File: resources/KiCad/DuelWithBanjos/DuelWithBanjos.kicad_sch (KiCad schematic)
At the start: 4 parts, among them U1 ESP32-WROOM-32

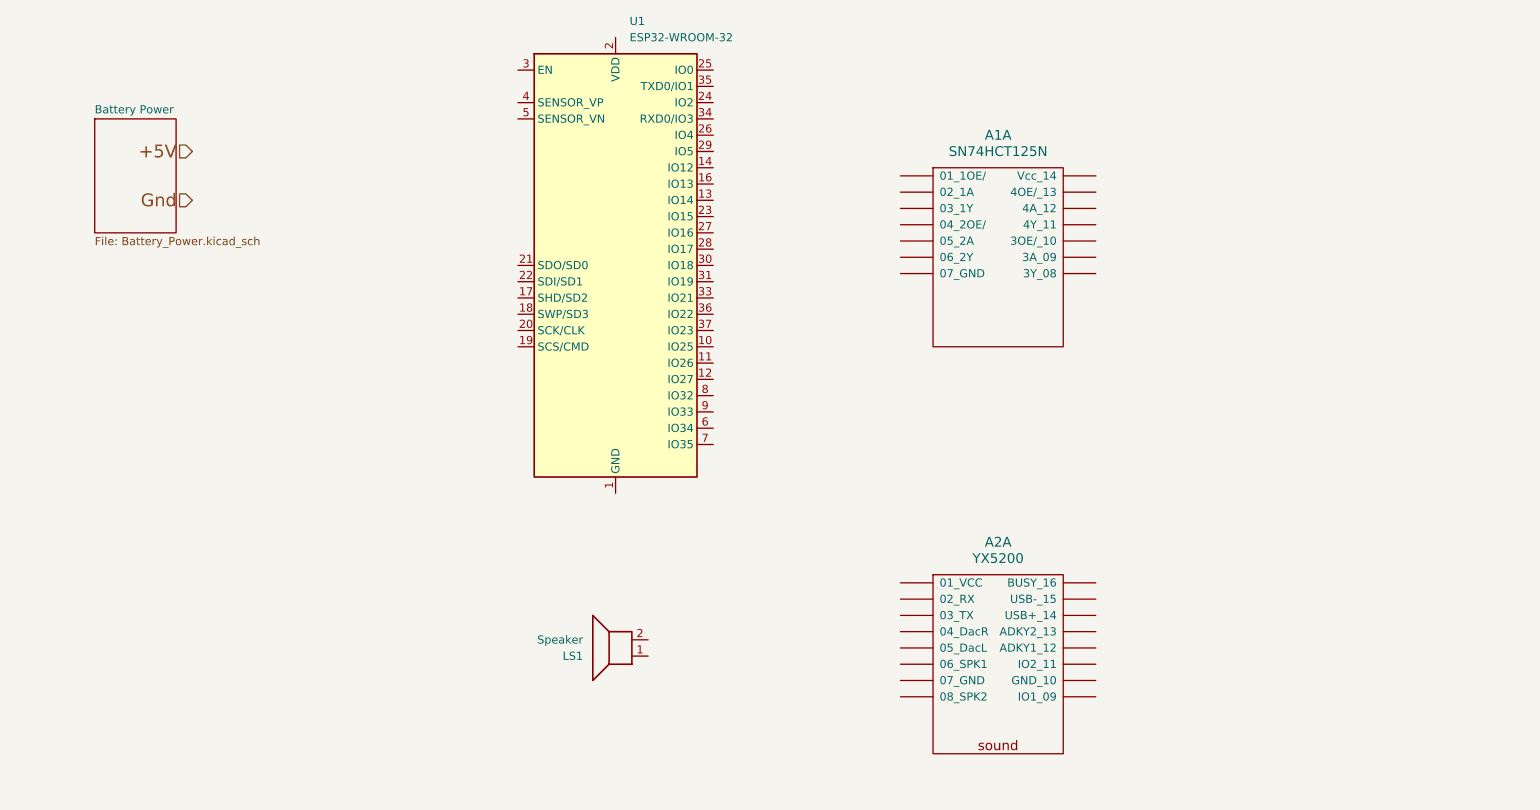
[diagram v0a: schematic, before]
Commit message: pin assignments and schematic first cut
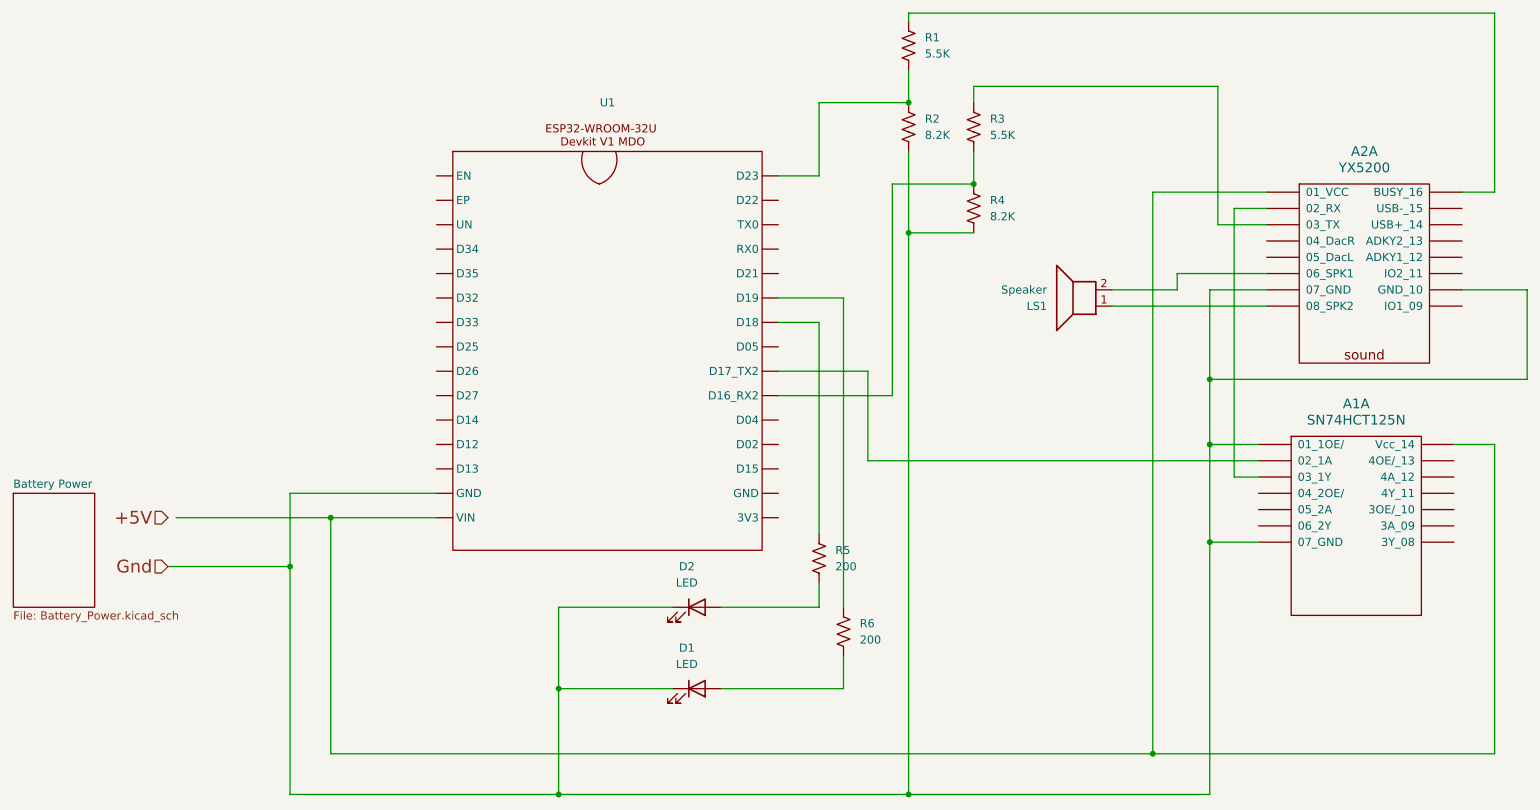
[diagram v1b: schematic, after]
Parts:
- removed U1: ESP32-WROOM-32, RF_Module:ESP32-WROOM-32, symbol RF_Module:ESP32-WROOM-32
- added D1, D2: LED, symbol Device:LED
- added R1, R3: 5.5K, symbol Device:R_US
- added R2, R4: 8.2K, symbol Device:R_US
- added R5, R6: 200, symbol Device:R_US
- added U1: ~, symbol mdoLibrary:mdo_esp32_wroom
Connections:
- net Gnd : now also A1.~ (Vcc_14), A2.~ (USB-_15), D1.1 (K), D2.1 (K), R2.2, R4.2, U1. (VIN)
- net at LS1.1: now also A2.~ (USB-_15)
- net at LS1.2: now also A2.~ (USB-_15)
- new net: R1.2, R2.1, U1. (VIN)
- new net: A2.~ (USB-_15), R3.1
- new net: R3.2, R4.1, U1. (VIN)
- new net: R5.1, U1. (VIN)
- new net: A1.~ (Vcc_14), U1. (VIN)
- new net: A1.~ (Vcc_14), A2.~ (USB-_15), U1. (VIN)
- new net: R6.1, U1. (VIN)
- new net: D2.2 (A), R5.2
- new net: A1.~ (Vcc_14), A2.~ (USB-_15)
- new net: A2.~ (USB-_15), R1.1
- new net: D1.2 (A), R6.2
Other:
- moved on the sheet: A1A, A2A, LS1

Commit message: update schematic
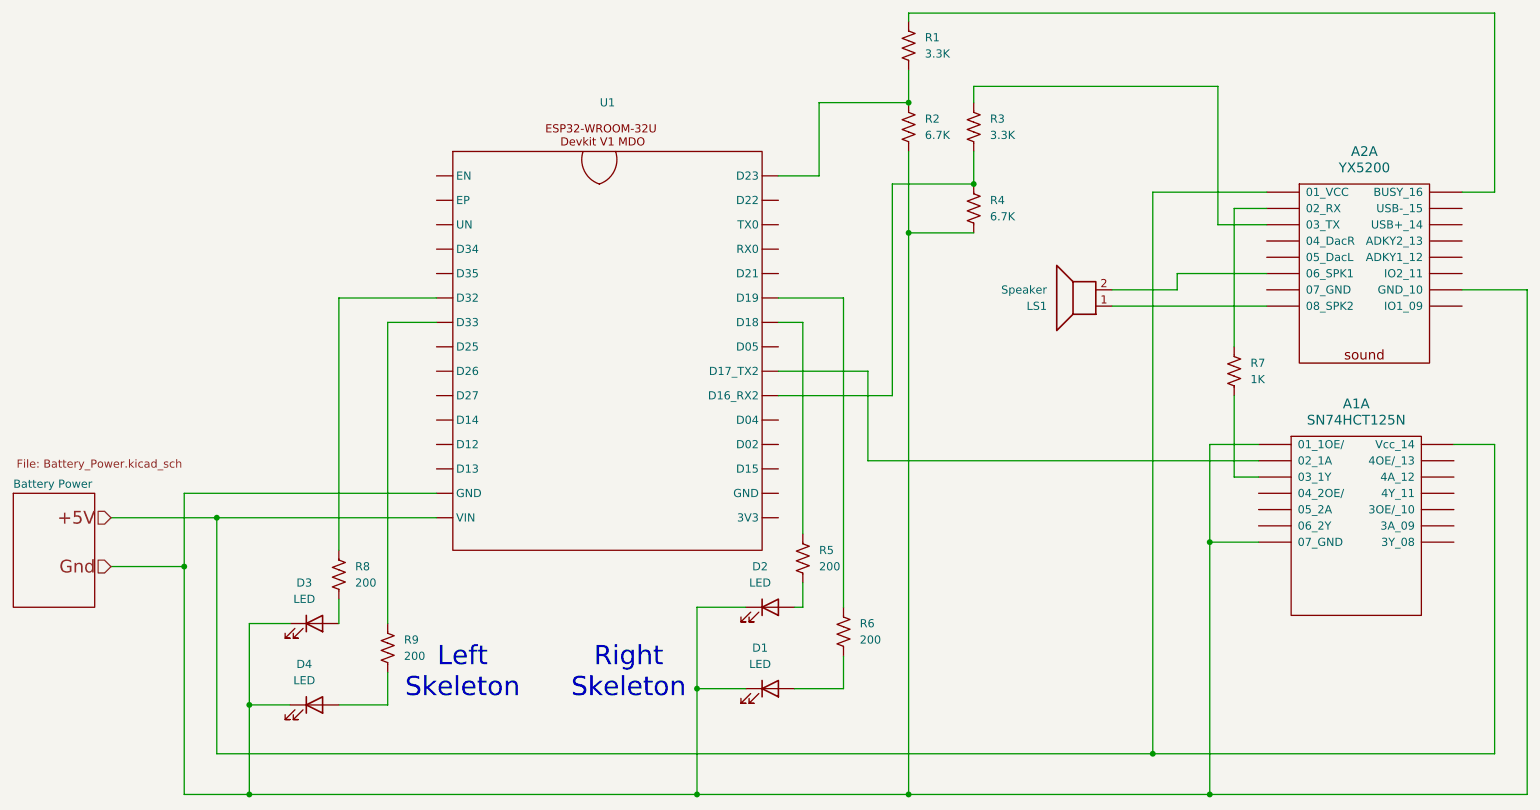
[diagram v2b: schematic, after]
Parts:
- added D3, D4: LED, symbol Device:LED
- added R7: 1K, symbol Device:R_US
- added R8, R9: 200, symbol Device:R_US
- R1, R3: value 5.5K -> 3.3K
- R2, R4: value 8.2K -> 6.7K
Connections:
- net +5V : now also A1.~ (Vcc_14), A2.~ (USB-_15), U1. (VIN)
- net Gnd : now also D3.1 (K), D4.1 (K)
- new net: R9.1, U1. (VIN)
- new net: D4.2 (A), R9.2
- new net: R8.1, U1. (VIN)
- new net: D3.2 (A), R8.2
- new net: A2.~ (USB-_15), R7.1
- new net: A1.~ (Vcc_14), R7.2
- new net: A1.~ (Vcc_14), U1. (VIN)
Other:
- note added: "Left Skeleton"
- note added: "Right Skeleton"
- moved on the sheet: D1, D2, R5

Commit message: add connectors for skeletons, move deck chairs around
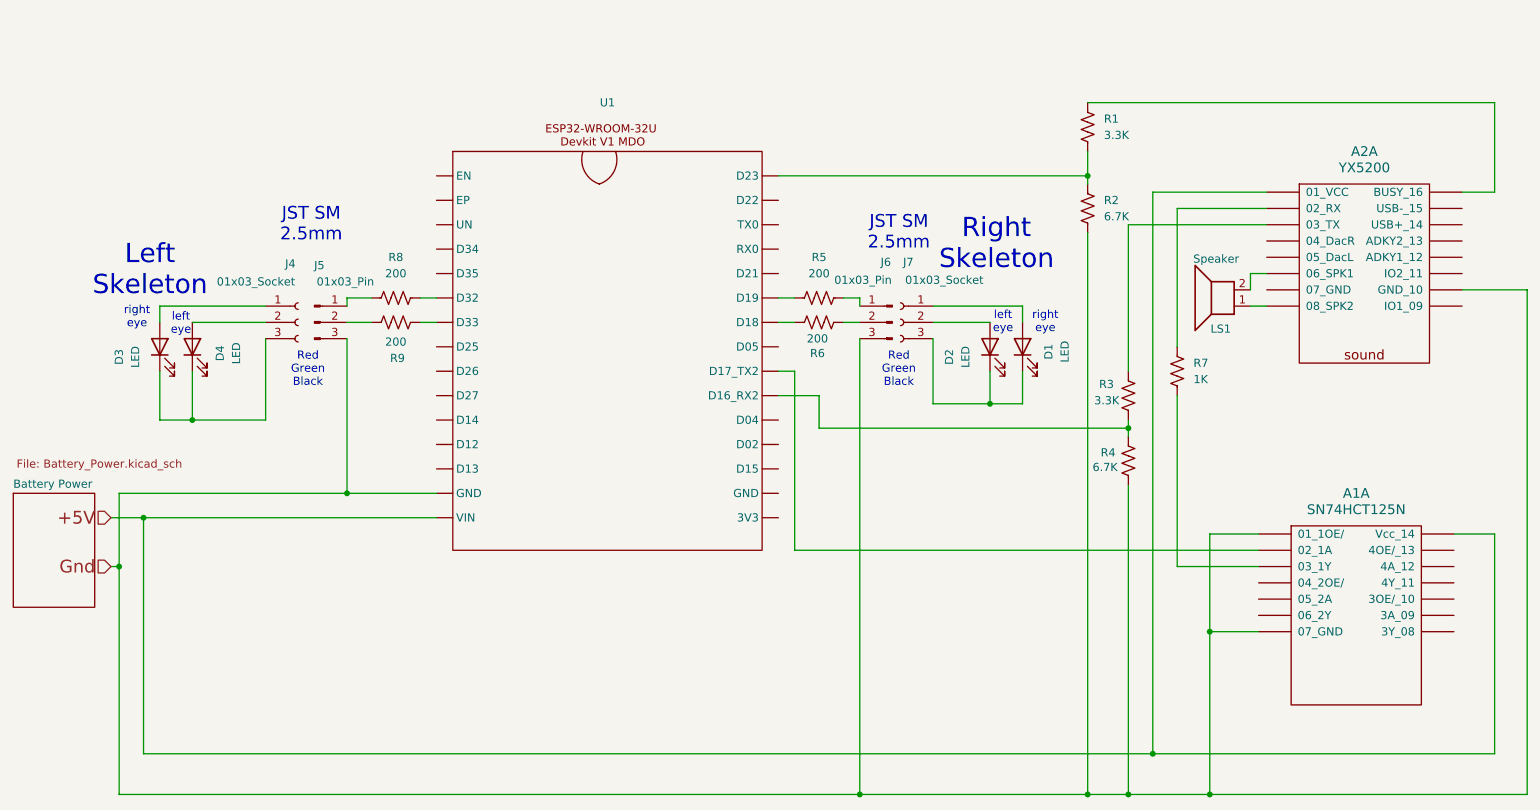
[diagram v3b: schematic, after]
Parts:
- added J4, J7: 01x03_Socket, symbol Connector:Conn_01x03_Socket
- added J5, J6: 01x03_Pin, symbol Connector:Conn_01x03_Pin
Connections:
- net Gnd : now also J5.3 (Pin_3), J6.3 (Pin_3); no longer D1.1 (K), D2.1 (K), D3.1 (K), D4.1 (K)
- net at R9.2: now also J5.2 (Pin_2); no longer D4.2 (A)
- net at R8.2: now also J5.1 (Pin_1); no longer D3.2 (A)
- net at R5.1: now also J6.1 (Pin_1); no longer U1. (VIN)
- net at R6.1: now also J6.2 (Pin_2); no longer U1. (VIN)
- net at R5.2: now also U1. (VIN); no longer D2.2 (A)
- net at R6.2: now also U1. (VIN); no longer D1.2 (A)
- new net: D3.1 (K), D4.1 (K), J4.3 (Pin_3)
- new net: D4.2 (A), J4.2 (Pin_2)
- new net: A1.~ (Vcc_14), U1. (VIN)
- new net: D3.2 (A), J4.1 (Pin_1)
- new net: D1.1 (K), D2.1 (K), J7.3 (Pin_3)
- new net: D2.2 (A), J7.2 (Pin_2)
- new net: D1.2 (A), J7.1 (Pin_1)
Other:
- note added: "JST SM 2.5mm"
- note added: "Red Green Black"
- note added: "left eye"
- note added: "right eye"
- moved on the sheet: A1A, D1, D2, D3, D4, LS1, R1, R2, R3, R4, R5, R6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

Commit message: move pins farther apart
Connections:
- new net: A1.~ (Vcc_14), U1. (VIN)
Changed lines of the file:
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@@
 	(title_block
 		(title "DuelWithBanjos")
-		(date "2025-04-10")
+		(date "2025-04-13")
 		(rev "Rev 0.9")
 		(company "https://github.com/Mark-MDO47")
@@
 	(wire
 		(pts
+			(xy 83.82 80.01) (xy 83.82 87.63)
+		)
+		(stroke
+			(width 0)
+			(type default)
+		)
+	)
+	(wire
+		(pts
 			(xy 187.96 53.34) (xy 187.96 57.15)
 		)
@@
 	(wire
 		(pts
+			(xy 86.36 87.63) (xy 83.82 87.63)
+		)
+		(stroke
+			(width 0)
+			(type default)
+		)
+	)
+	(wire
+		(pts
 			(xy 36.83 118.11) (xy 36.83 153.67)
 		)
 		(stroke
-			(width 0)
-			(type default)
-		)
-	)
-	(wire
-		(pts
-			(xy 83.82 80.01) (xy 86.36 80.01)
-		)
-		(stroke

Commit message: KiCad V9.0.1
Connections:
- new net: A1.~ (3Y_08), U1. (3V3)
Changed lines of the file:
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@@
 (kicad_sch
-	(version 20231120)
+	(version 20250114)
 	(generator "eeschema")
-	(generator_version "8.0")
+	(generator_version "9.0")
 	(paper "USLetter")
 	(title_block
 		(title "DuelWithBanjos")
-		(date "2025-04-13")
+		(date "2025-05-08")
 		(rev "Rev 0.9")
 		(company "https://github.com/Mark-MDO47")
 	)
+	(text "Red\nGreen\nBlack"
+		(exclude_from_sim no)
+		(at 66.294 87.376 0)
+		(effects
+			(font
+				(size 1.27 1.27)
+			)
+		)
+	)
+	(text "Right\nSkeleton"
+		(exclude_from_sim no)
+		(at 173.736 67.818 0)
+		(effects
+			(font
+				(size 3 3)
+			)
+		)
+	)
+	(text "right\neye"
+		(exclude_from_sim no)
+		(at 39.624 79.248 0)
+		(effects
+			(font
+				(size 1.27 1.27)
+			)
+		)
+	)
+	(text "left\neye"
+		(exclude_from_sim no)
+		(at 46.482 80.264 0)
+		(effects
+			(font
+				(size 1.27 1.27)
+			)
+		)
+	)
+	(text "JST SM\n2.5mm"
+		(exclude_from_sim no)
+		(at 158.496 66.04 0)
+		(effects
+			(font
+				(size 2 2)
+			)
+		)
+	)
+	(text "left\neye"
+		(exclude_from_sim no)
+		(at 174.752 80.01 0)
+		(effects
+			(font
+				(size 1.27 1.27)
+			)
+		)
+	)
+	(text "JST SM\n2.5mm"
+		(exclude_from_sim no)
+		(at 66.802 64.77 0)
+		(effects
+			(font
+				(size 2 2)
+			)
+		)
+	)
+	(text "Red\nGreen\nBlack"
+		(exclude_from_sim no)
+		(at 158.496 87.376 0)
+		(effects
+			(font
+				(size 1.27 1.27)
+			)
+		)
+	)
+	(text "right\neye"
+		(exclude_from_sim no)
+		(at 181.356 80.01 0)
+		(effects
+			(font
+				(size 1.27 1.27)
+			)
+		)
+	)
+	(text "Left\nSkeleton"
+		(exclude_from_sim no)
+		(at 41.656 71.882 0)
+		(effects
+			(font
+				(size 3 3)
+			)
+		)
+	)
 	(junction
 		(at 152.4 153.67)
@@
 		)
 	)
-	(text "Red\nGreen\nBlack"
-		(exclude_from_sim no)
-		(at 66.294 87.376 0)
-		(effects
-			(font
-				(size 1.27 1.27)
-			)
-		)
-	)
-	(text "Right\nSkeleton"
-		(exclude_from_sim no)
-		(at 173.736 67.818 0)
-		(effects
-			(font
-				(size 3 3)
-			)
-		)
-	)
-	(text "right\neye"
-		(exclude_from_sim no)
-		(at 39.624 79.248 0)
-		(effects
-			(font
-				(size 1.27 1.27)
-			)
-		)
-	)
-	(text "left\neye"
-		(exclude_from_sim no)
-		(at 46.482 80.264 0)
-		(effects
-			(font
-				(size 1.27 1.27)
-			)
-		)
-	)
-	(text "JST SM\n2.5mm"
-		(exclude_from_sim no)
-		(at 158.496 66.04 0)
-		(effects
-			(font
-				(size 2 2)
-			)
-		)
-	)
-	(text "left\neye"
-		(exclude_from_sim no)
-		(at 174.752 80.01 0)
-		(effects
-			(font
-				(size 1.27 1.27)
-			)
-		)
-	)
-	(text "JST SM\n2.5mm"
-		(exclude_from_sim no)
-		(at 66.802 64.77 0)
-		(effects
-			(font
-				(size 2 2)
-			)
-		)
-	)
-	(text "Red\nGreen\nBlack"
-		(exclude_from_sim no)
-		(at 158.496 87.376 0)
-		(effects
-			(font
-				(size 1.27 1.27)
-			)
-		)
-	)
-	(text "right\neye"
-		(exclude_from_sim no)
-		(at 181.356 80.01 0)
-		(effects
-			(font
-				(size 1.27 1.27)
-			)
-		)
-	)
-	(text "Left\nSkeleton"
-		(exclude_from_sim no)
-		(at 41.656 71.882 0)
-		(effects
-			(font
-				(size 3 3)
-			)
-		)
-	)
 	(hierarchical_label "+5V "
 		(shape input)
 		(at 35.56 110.49 180)
-		(fields_autoplaced yes)
 		(effects
 			(font
@@
 		(shape input)
 		(at 35.56 118.11 180)
-		(fields_autoplaced yes)
 		(effects
 			(font
@@
 		(at 20.32 106.68)
 		(size 12.7 17.78)
+		(exclude_from_sim no)
+		(in_bom yes)
+		(on_board yes)
+		(dnp no)
 		(stroke
 			(width 0.1524)
@@
 		)
 	)
+	(embedded_fonts no)
 )

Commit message: V1.0 schematic power update
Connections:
- new net: A1.~ (3Y_08), U1. (3V3)
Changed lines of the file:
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@@
 	(title_block
 		(title "DuelWithBanjos")
-		(date "2025-05-08")
-		(rev "Rev 0.9")
+		(date "2025-06-08")
+		(rev "Rev 1.0")
 		(company "https://github.com/Mark-MDO47")
 	)
